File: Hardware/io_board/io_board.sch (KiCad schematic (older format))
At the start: 12 parts, among them J1 Conn_01x40, J2 Conn_02x05_Odd_Even, J3 Mini-DIN-6, J4 Conn_02x10_Odd_Even, U1 74LS137, U2 W65C22NxP

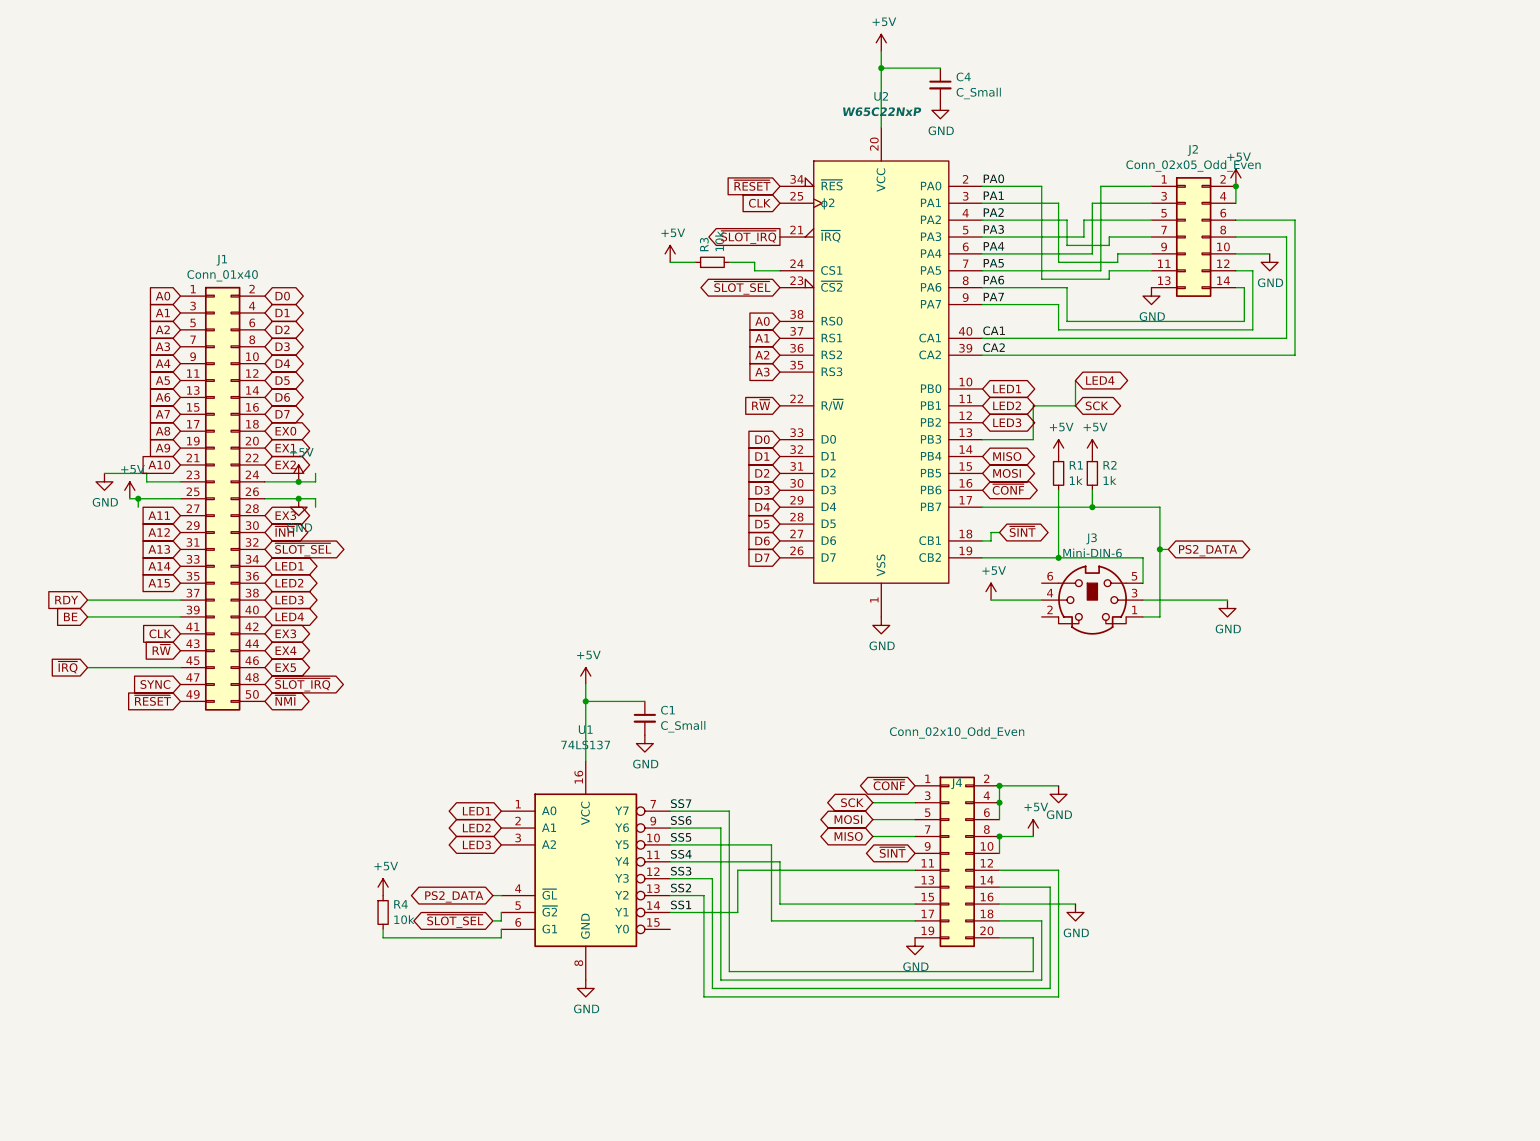
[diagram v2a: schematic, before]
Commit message: pin legends
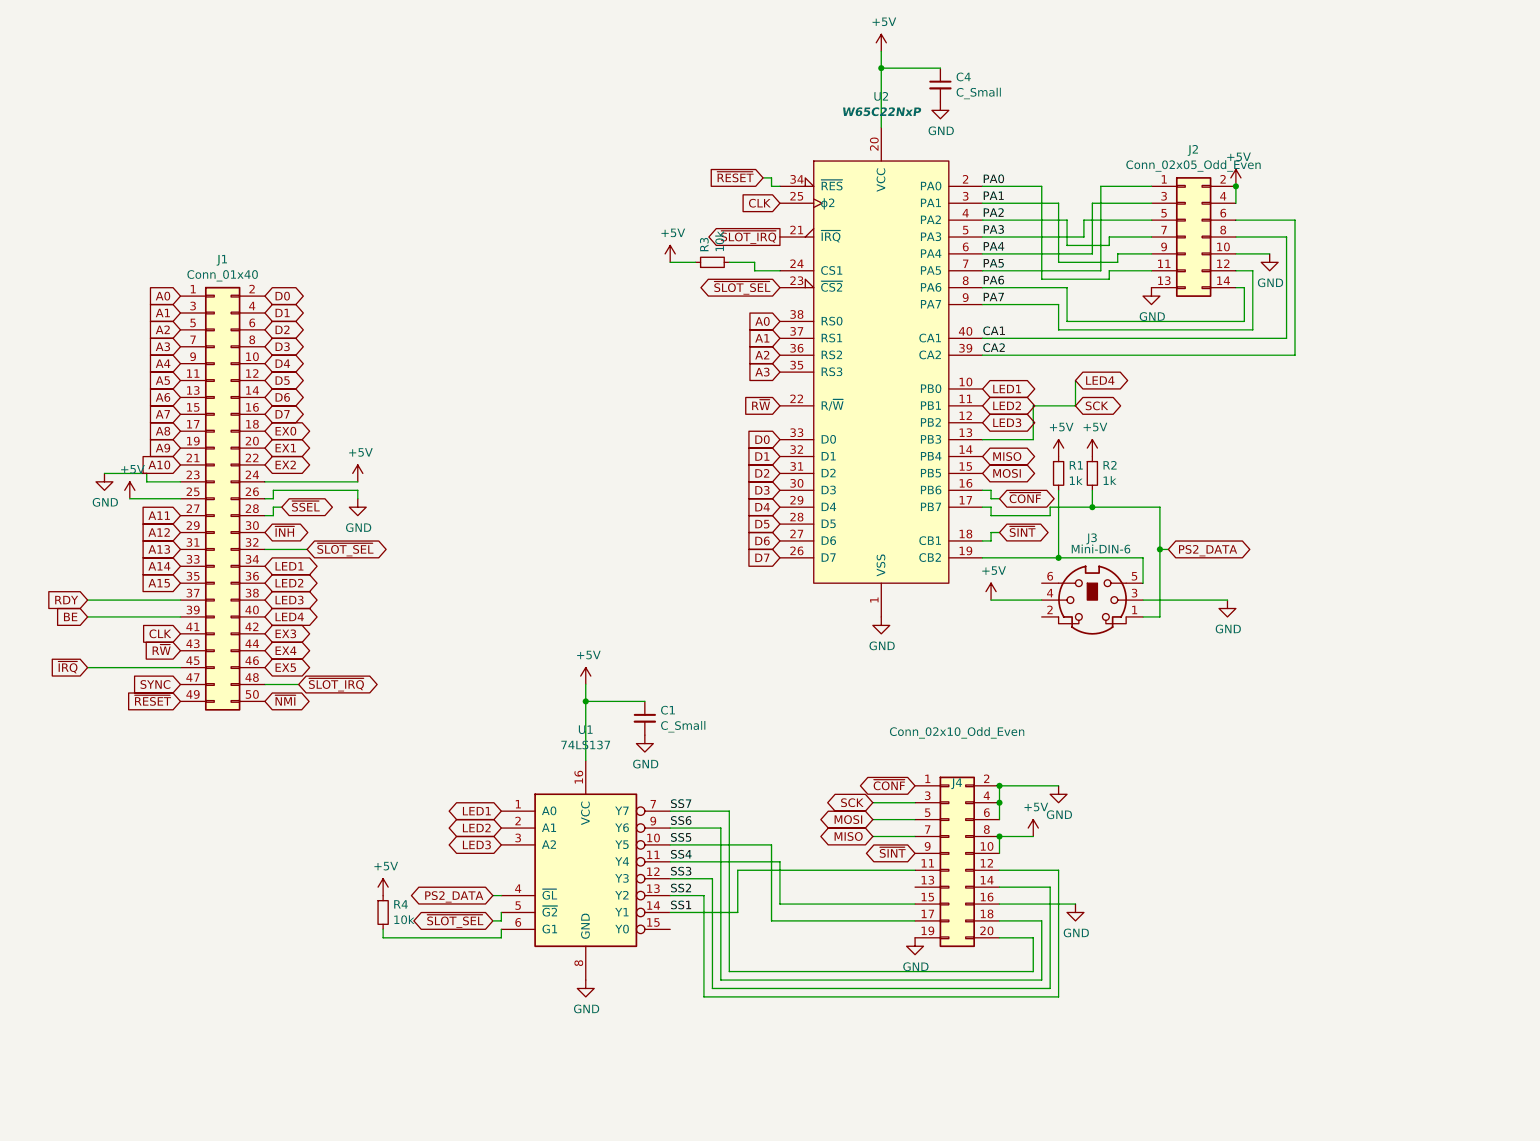
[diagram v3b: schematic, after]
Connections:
- net EX3: no longer J1.28 (Pin_28)
- new net ~SSEL~: J1.28 (Pin_28)
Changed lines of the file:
@@
 L power:+5V #PWR0101
 U 1 1 5FD64472
-P 3000 3350
-F 0 "#PWR0101" H 3000 3200 50  0001 C CNN
-F 1 "+5V" H 3015 3523 50  0000 C CNN
-F 2 "" H 3000 3350 50  0001 C CNN
-F 3 "" H 3000 3350 50  0001 C CNN
-	1    3000 3350
-	1    0    0    -1
-$EndComp
-Wire Wire Line
-	3000 3350 2800 3350
+P 3350 3350
+F 0 "#PWR0101" H 3350 3200 50  0001 C CNN
+F 1 "+5V" H 3365 3523 50  0000 C CNN
+F 2 "" H 3350 3350 50  0001 C CNN
+F 3 "" H 3350 3350 50  0001 C CNN
+	1    3350 3350
+	1    0    0    -1
+$EndComp
 $Comp
 L power:+5V #PWR0102
@@
 	1    0    0    -1
 $EndComp
-Wire Wire Line
-	2300 3450 2050 3450
 $Comp
 L power:GND #PWR0103
 U 1 1 5FD65E00
-P 3000 3450
-F 0 "#PWR0103" H 3000 3200 50  0001 C CNN
-F 1 "GND" H 3005 3277 50  0000 C CNN
-F 2 "" H 3000 3450 50  0001 C CNN
-F 3 "" H 3000 3450 50  0001 C CNN
-	1    3000 3450
-	1    0    0    -1
-$EndComp
-Wire Wire Line
-	3000 3450 2800 3450
+P 3350 3450
+F 0 "#PWR0103" H 3350 3200 50  0001 C CNN
+F 1 "GND" H 3355 3277 50  0000 C CNN
+F 2 "" H 3350 3450 50  0001 C CNN
+F 3 "" H 3350 3450 50  0001 C CNN
+	1    3350 3450
+	1    0    0    -1
+$EndComp
 $Comp
 L power:GND #PWR0104
@@
 Text GLabel 1750 4450 0    50   Input ~ 0
 ~IRQ~
-Text GLabel 2800 4550 2    50   BiDi ~ 0
+Text GLabel 3000 4550 2    50   BiDi ~ 0
 ~SLOT_IRQ~
 Text GLabel 2800 4450 2    50   BiDi ~ 0
@@
 EX3
 Wire Wire Line
-	3100 3300 3100 3350
-Wire Wire Line
-	3100 3350 3000 3350
-Connection ~ 3000 3350
-Wire Wire Line
-	3100 3500 3100 3450
-Wire Wire Line
-	3100 3450 3000 3450
-Connection ~ 3000 3450
-Wire Wire Line
-	2050 3500 2050 3450
-Connection ~ 2050 3450
-Wire Wire Line
-	2050 3450 2000 3450
-Wire Wire Line
 	1750 4450 2300 4450
 Wire Wire Line
@@
 Wire Wire Line
 	1750 4150 2300 4150
-Text GLabel 2800 3550 2    50   BiDi ~ 0
-EX3
+Text GLabel 2900 3500 2    50   BiDi ~ 0
+~SSEL~
 Text GLabel 2800 3650 2    50   BiDi ~ 0
 ~INH~
-Text GLabel 2800 3750 2    50   BiDi ~ 0
+Text GLabel 3050 3750 2    50   BiDi ~ 0
 ~SLOT_SEL~
 Text GLabel 2800 3850 2    50   BiDi ~ 0
@@
 P 7700 4050
 F 0 "J3" H 7700 4417 50  0000 C CNN
-F 1 "Mini-DIN-6" H 7700 4326 50  0000 C CNN
+F 1 "Mini-DIN-6" H 7750 4350 50  0000 C CNN
 F 2 "mini-din:MINI-DIN-6-FULL-SHIELD" H 7700 4050 50  0001 C CNN
 F 3 "http://service.powerdynamics.com/ec/Catalog17/Section%2011.pdf" H 7700 4050 50  0001 C CNN
@@
 Text GLabel 5850 1700 0    50   Input ~ 0
 CLK
-Text GLabel 5850 1600 0    50   Input ~ 0
+Text GLabel 5750 1550 0    50   Input ~ 0
 ~RESET~
 Text GLabel 5850 1900 0    50   Output ~ 0
@@
 Wire Wire Line
 	7700 3400 7700 3500
-Connection ~ 7700 3500
-Wire Wire Line
-	7700 3500 7050 3500
 $Comp
 L Device:R_Small R1
@@
 Text GLabel 7050 3300 2    50   BiDi ~ 0
 MOSI
-Text GLabel 7050 3400 2    50   BiDi ~ 0
+Text GLabel 7150 3450 2    50   BiDi ~ 0
 ~CONF~
 $Comp
@@
 Text Label 5200 5300 0    50   ~ 0
 SS7
+Wire Wire Line
+	2800 3350 3350 3350
+Wire Wire Line
+	2800 3450 2850 3450
+Wire Wire Line
+	3050 3750 2800 3750
+Wire Wire Line
+	2000 3450 2300 3450
+Wire Wire Line
+	3000 4550 2800 4550
+Wire Wire Line
+	2900 3500 2850 3500
+Wire Wire Line
+	2850 3500 2850 3550
+Wire Wire Line
+	2850 3550 2800 3550
+Wire Wire Line
+	7150 3450 7100 3450
+Wire Wire Line
+	7100 3450 7100 3400
+Wire Wire Line
+	7100 3400 7050 3400
+Wire Wire Line
+	7700 3500 7450 3500
+Wire Wire Line
+	7450 3500 7450 3550
+Wire Wire Line
+	7450 3550 7100 3550
+Wire Wire Line
+	7100 3550 7100 3500
+Wire Wire Line
+	7100 3500 7050 3500
+Connection ~ 7700 3500
+Wire Wire Line
+	5750 1550 5800 1550
+Wire Wire Line
+	5800 1550 5800 1600
+Wire Wire Line
+	5800 1600 5850 1600
+Wire Wire Line
+	3350 3450 3350 3400
+Wire Wire Line
+	3350 3400 2850 3400
+Wire Wire Line
+	2850 3400 2850 3450
 $EndSCHEMATC

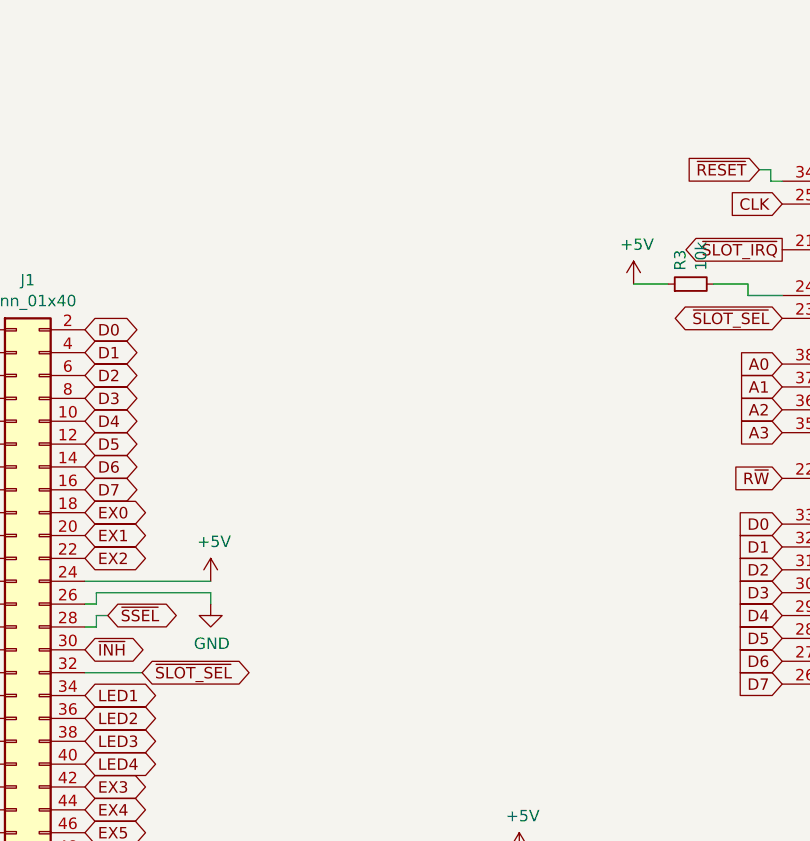
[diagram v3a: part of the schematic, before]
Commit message: Add LEDs to IO board
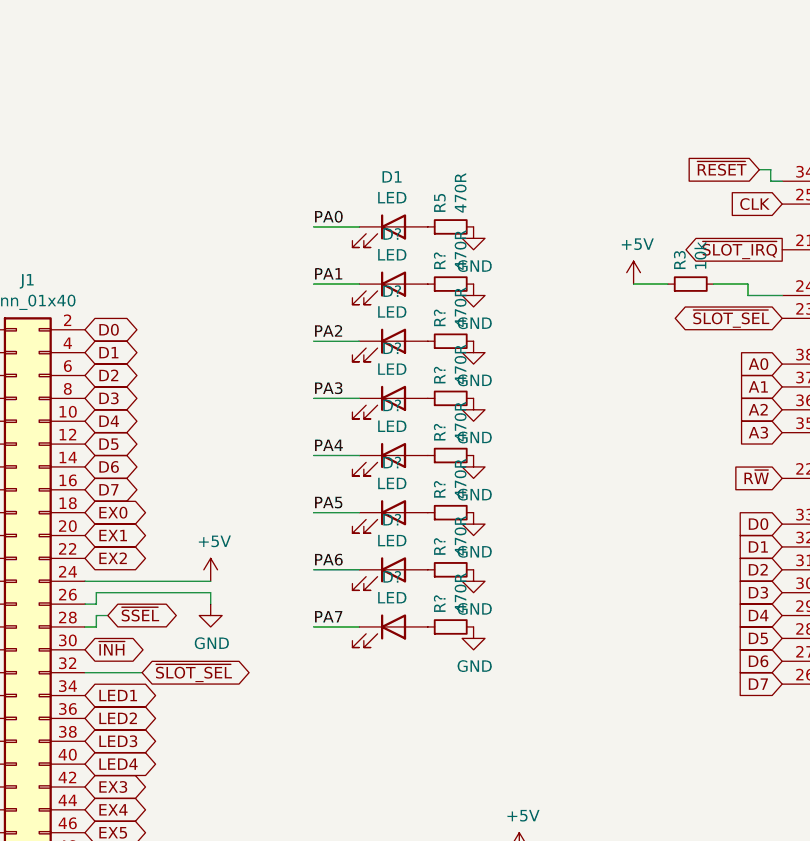
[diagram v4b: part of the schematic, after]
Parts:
- added D1, D? (x7): LED, LED_SMD:LED_1206_3216Metric_Pad1.42x1.75mm_HandSolder, symbol Device:LED
- added R5, R? (x7): 470R, Resistor_SMD:R_0805_2012Metric_Pad1.15x1.40mm_HandSolder, symbol Device:R_Small
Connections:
- net GND: now also R5.2, R?.2, R?.2, R?.2, R?.2, R?.2, R?.2, R?.2
- net PA0: now also D1.1 (K)
- net PA1: now also D?.1 (K)
- net PA2: now also D?.1 (K)
- net PA3: now also D?.1 (K)
- net PA4: now also D?.1 (K)
- net PA5: now also D?.1 (K)
- net PA6: now also D?.1 (K)
- net PA7: now also D?.1 (K)
- new net: D1.2 (A), R5.1
- new net: D?.2 (A), R?.1 (x7)

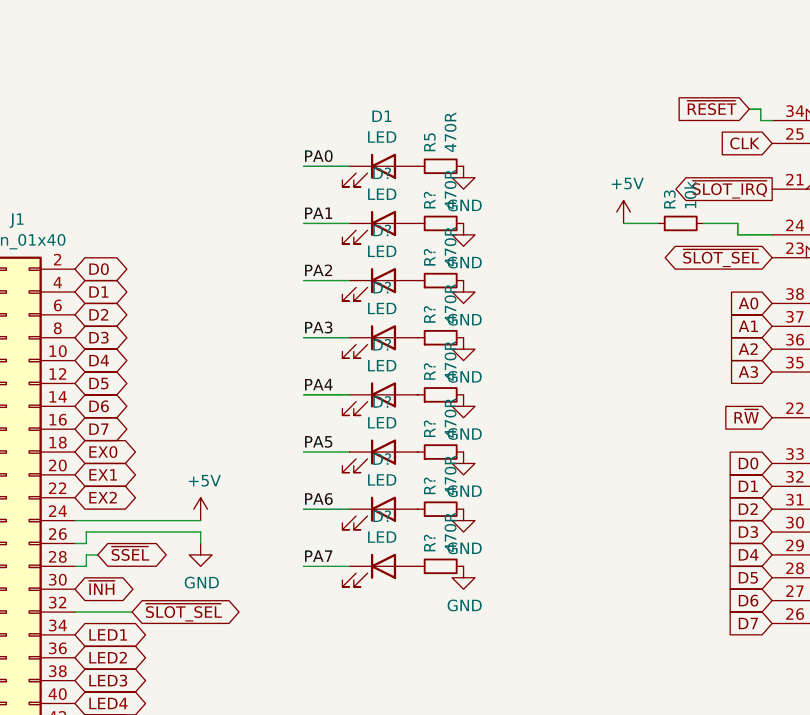
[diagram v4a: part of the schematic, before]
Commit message: Update io board 3D view
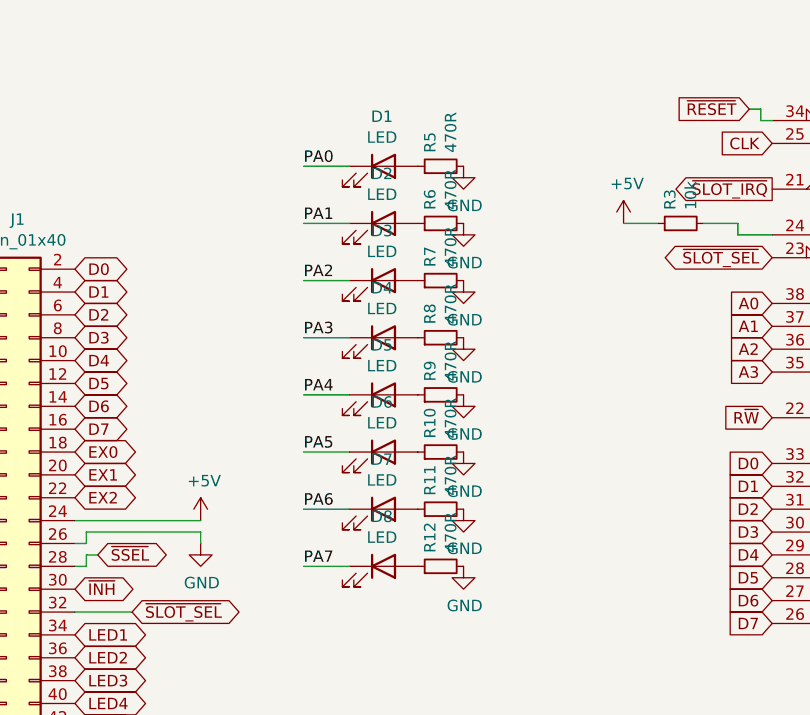
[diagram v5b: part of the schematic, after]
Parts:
- gave numbers to parts that had none: 14
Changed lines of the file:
@@
 	4000 1800 3800 1800
 $Comp
-L Device:LED D?
+L Device:LED D2
 U 1 1 5FF4DDFD
 P 4150 2050
-F 0 "D?" H 4143 2267 50  0000 C CNN
+F 0 "D2" H 4143 2267 50  0000 C CNN
 F 1 "LED" H 4143 2176 50  0000 C CNN
 F 2 "LED_SMD:LED_1206_3216Metric_Pad1.42x1.75mm_HandSolder" H 4150 2050 50  0001 C CNN
@@
 $EndComp
 $Comp
-L Device:R_Small R?
+L Device:R_Small R6
 U 1 1 5FF4DE03
 P 4400 2050
-F 0 "R?" H 4459 2096 50  0000 L CNN
+F 0 "R6" H 4459 2096 50  0000 L CNN
 F 1 "470R" H 4459 2005 50  0000 L CNN
 F 2 "Resistor_SMD:R_0805_2012Metric_Pad1.15x1.40mm_HandSolder" H 4400 2050 50  0001 C CNN
@@
 $EndComp
 $Comp
-L power:GND #PWR?
+L power:GND #PWR0110
 U 1 1 5FF4DE09
 P 4500 2050
-F 0 "#PWR?" H 4500 1800 50  0001 C CNN
+F 0 "#PWR0110" H 4500 1800 50  0001 C CNN
 F 1 "GND" H 4505 1877 50  0000 C CNN
 F 2 "" H 4500 2050 50  0001 C CNN
@@
 	4000 2050 3800 2050
 $Comp
-L Device:LED D?
+L Device:LED D3
 U 1 1 5FF55550
 P 4150 2300
-F 0 "D?" H 4143 2517 50  0000 C CNN
+F 0 "D3" H 4143 2517 50  0000 C CNN
 F 1 "LED" H 4143 2426 50  0000 C CNN
 F 2 "LED_SMD:LED_1206_3216Metric_Pad1.42x1.75mm_HandSolder" H 4150 2300 50  0001 C CNN
@@
 $EndComp
 $Comp
-L Device:R_Small R?
+L Device:R_Small R7
 U 1 1 5FF55556
 P 4400 2300
-F 0 "R?" H 4459 2346 50  0000 L CNN
+F 0 "R7" H 4459 2346 50  0000 L CNN
 F 1 "470R" H 4459 2255 50  0000 L CNN
 F 2 "Resistor_SMD:R_0805_2012Metric_Pad1.15x1.40mm_HandSolder" H 4400 2300 50  0001 C CNN
@@
 $EndComp
 $Comp
-L power:GND #PWR?
+L power:GND #PWR0115
 U 1 1 5FF5555C
 P 4500 2300
-F 0 "#PWR?" H 4500 2050 50  0001 C CNN
+F 0 "#PWR0115" H 4500 2050 50  0001 C CNN
 F 1 "GND" H 4505 2127 50  0000 C CNN
 F 2 "" H 4500 2300 50  0001 C CNN
@@
 	4000 2300 3800 2300
 $Comp
-L Device:LED D?
+L Device:LED D4
 U 1 1 5FF5CDD6
 P 4150 2550
-F 0 "D?" H 4143 2767 50  0000 C CNN
+F 0 "D4" H 4143 2767 50  0000 C CNN
 F 1 "LED" H 4143 2676 50  0000 C CNN
 F 2 "LED_SMD:LED_1206_3216Metric_Pad1.42x1.75mm_HandSolder" H 4150 2550 50  0001 C CNN
@@
 $EndComp
 $Comp
-L Device:R_Small R?
+L Device:R_Small R8
 U 1 1 5FF5CDDC
 P 4400 2550
-F 0 "R?" H 4459 2596 50  0000 L CNN
+F 0 "R8" H 4459 2596 50  0000 L CNN
 F 1 "470R" H 4459 2505 50  0000 L CNN
 F 2 "Resistor_SMD:R_0805_2012Metric_Pad1.15x1.40mm_HandSolder" H 4400 2550 50  0001 C CNN
@@
 $EndComp
 $Comp
-L power:GND #PWR?
+L power:GND #PWR0116
 U 1 1 5FF5CDE2
 P 4500 2550
-F 0 "#PWR?" H 4500 2300 50  0001 C CNN
+F 0 "#PWR0116" H 4500 2300 50  0001 C CNN
 F 1 "GND" H 4505 2377 50  0000 C CNN
 F 2 "" H 4500 2550 50  0001 C CNN
@@
 	4000 2550 3800 2550
 $Comp
-L Device:LED D?
+L Device:LED D5
 U 1 1 5FF64552
 P 4150 2800
-F 0 "D?" H 4143 3017 50  0000 C CNN
+F 0 "D5" H 4143 3017 50  0000 C CNN
 F 1 "LED" H 4143 2926 50  0000 C CNN
 F 2 "LED_SMD:LED_1206_3216Metric_Pad1.42x1.75mm_HandSolder" H 4150 2800 50  0001 C CNN
@@
 $EndComp
 $Comp
-L Device:R_Small R?
+L Device:R_Small R9
 U 1 1 5FF64558
 P 4400 2800
-F 0 "R?" H 4459 2846 50  0000 L CNN
+F 0 "R9" H 4459 2846 50  0000 L CNN
 F 1 "470R" H 4459 2755 50  0000 L CNN
 F 2 "Resistor_SMD:R_0805_2012Metric_Pad1.15x1.40mm_HandSolder" H 4400 2800 50  0001 C CNN
@@
 $EndComp
 $Comp
-L power:GND #PWR?
+L power:GND #PWR0128
 U 1 1 5FF6455E
 P 4500 2800
-F 0 "#PWR?" H 4500 2550 50  0001 C CNN
+F 0 "#PWR0128" H 4500 2550 50  0001 C CNN
 F 1 "GND" H 4505 2627 50  0000 C CNN
 F 2 "" H 4500 2800 50  0001 C CNN
@@
 	4000 2800 3800 2800
 $Comp
-L Device:LED D?
+L Device:LED D6
 U 1 1 5FF6C107
 P 4150 3050
-F 0 "D?" H 4143 3267 50  0000 C CNN
+F 0 "D6" H 4143 3267 50  0000 C CNN
 F 1 "LED" H 4143 3176 50  0000 C CNN
 F 2 "LED_SMD:LED_1206_3216Metric_Pad1.42x1.75mm_HandSolder" H 4150 3050 50  0001 C CNN
@@
 $EndComp
 $Comp
-L Device:R_Small R?
+L Device:R_Small R10
 U 1 1 5FF6C10D
 P 4400 3050
-F 0 "R?" H 4459 3096 50  0000 L CNN
+F 0 "R10" H 4459 3096 50  0000 L CNN
 F 1 "470R" H 4459 3005 50  0000 L CNN
 F 2 "Resistor_SMD:R_0805_2012Metric_Pad1.15x1.40mm_HandSolder" H 4400 3050 50  0001 C CNN
@@
 $EndComp
 $Comp
-L power:GND #PWR?
+L power:GND #PWR0129
 U 1 1 5FF6C113
 P 4500 3050
-F 0 "#PWR?" H 4500 2800 50  0001 C CNN
+F 0 "#PWR0129" H 4500 2800 50  0001 C CNN
 F 1 "GND" H 4505 2877 50  0000 C CNN
 F 2 "" H 4500 3050 50  0001 C CNN
@@
 	4000 3050 3800 3050
 $Comp
-L Device:LED D?
+L Device:LED D7
 U 1 1 5FF73AB8
 P 4150 3300
-F 0 "D?" H 4143 3517 50  0000 C CNN
+F 0 "D7" H 4143 3517 50  0000 C CNN
 F 1 "LED" H 4143 3426 50  0000 C CNN
 F 2 "LED_SMD:LED_1206_3216Metric_Pad1.42x1.75mm_HandSolder" H 4150 3300 50  0001 C CNN
@@
 $EndComp
 $Comp
-L Device:R_Small R?
+L Device:R_Small R11
 U 1 1 5FF73ABE
 P 4400 3300
-F 0 "R?" H 4459 3346 50  0000 L CNN
+F 0 "R11" H 4459 3346 50  0000 L CNN
 F 1 "470R" H 4459 3255 50  0000 L CNN
 F 2 "Resistor_SMD:R_0805_2012Metric_Pad1.15x1.40mm_HandSolder" H 4400 3300 50  0001 C CNN
@@
 $EndComp
 $Comp
-L power:GND #PWR?
+L power:GND #PWR0130
 U 1 1 5FF73AC4
 P 4500 3300
-F 0 "#PWR?" H 4500 3050 50  0001 C CNN
+F 0 "#PWR0130" H 4500 3050 50  0001 C CNN
 F 1 "GND" H 4505 3127 50  0000 C CNN
 F 2 "" H 4500 3300 50  0001 C CNN
@@
 	4000 3300 3800 3300
 $Comp
-L Device:LED D?
+L Device:LED D8
 U 1 1 5FF7B8A8
 P 4150 3550
-F 0 "D?" H 4143 3767 50  0000 C CNN
+F 0 "D8" H 4143 3767 50  0000 C CNN
 F 1 "LED" H 4143 3676 50  0000 C CNN
 F 2 "LED_SMD:LED_1206_3216Metric_Pad1.42x1.75mm_HandSolder" H 4150 3550 50  0001 C CNN
@@
 $EndComp
 $Comp
-L Device:R_Small R?
+L Device:R_Small R12
 U 1 1 5FF7B8AE
 P 4400 3550
-F 0 "R?" H 4459 3596 50  0000 L CNN
+F 0 "R12" H 4459 3596 50  0000 L CNN
 F 1 "470R" H 4459 3505 50  0000 L CNN
 F 2 "Resistor_SMD:R_0805_2012Metric_Pad1.15x1.40mm_HandSolder" H 4400 3550 50  0001 C CNN
@@
 $EndComp
 $Comp
-L power:GND #PWR?
+L power:GND #PWR0131
 U 1 1 5FF7B8B4
 P 4500 3550
-F 0 "#PWR?" H 4500 3300 50  0001 C CNN
+F 0 "#PWR0131" H 4500 3300 50  0001 C CNN
 F 1 "GND" H 4505 3377 50  0000 C CNN
 F 2 "" H 4500 3550 50  0001 C CNN
